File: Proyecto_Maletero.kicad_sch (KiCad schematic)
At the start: 28 parts, among them J2 Conn_01x02, J3 Conn_01x02, J4 Conn_01x03, J5 Conn_01x02, J6 Conn_01x02, J7 Conn_01x03, SW1 SW_Push, SW2 SW_SPDT, U1 LT1117-ADJ, U2 MCP2551-I-SN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

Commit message: Correccion de errores
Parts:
- removed SW2: SW_SPDT, symbol Switch:SW_SPDT
- added J8: Conn_01x02, symbol Connector_Generic:Conn_01x02
- added SW3: SW_SPST, symbol Switch:SW_SPST
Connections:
- net VRth: now also J8.1 (Pin_1), SW3.2 (B)
- net Vin: now reaches R1.2
- net Vin: now also J8.2 (Pin_2), SW3.1 (A)
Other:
- note added: "Pines switch calefactor"
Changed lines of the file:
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@@
 		)
 	)
+	(text "Pines switch \ncalefactor"
+		(exclude_from_sim no)
+		(at 116.332 30.988 0)
+		(effects
+			(font
+				(size 1.27 1.27)
+			)
+		)
+	)
 	(text "Activar Rth"
 		(exclude_from_sim no)
@@
 	)
 	(junction
+		(at 166.37 184.15)
+		(diameter 0)
+		(color 0 0 0 0)
+	)
+	(junction
 		(at 102.87 83.82)
 		(diameter 0)
@@
 	)
 	(junction
+		(at 156.21 184.15)
+		(diameter 0)
+		(color 0 0 0 0)
+	)
+	(junction
 		(at 107.95 83.82)
 		(diameter 0)
@@
 	(wire
 		(pts
+			(xy 166.37 184.15) (xy 166.37 179.07)
+		)
+		(stroke
+			(width 0)
+			(type default)
+		)
+	)
+	(wire
+		(pts
 			(xy 199.39 30.48) (xy 207.01 30.48)
 		)
@@
 	(wire
 		(pts
+			(xy 166.37 184.15) (xy 168.91 184.15)
+		)
+		(stroke
+			(width 0)
+			(type default)
+		)
+	)
+	(wire
+		(pts
 			(xy 119.38 102.87) (xy 120.65 102.87)
 		)
@@
 	(wire
 		(pts
-			(xy 166.37 181.61) (xy 168.91 181.61)
+			(xy 24.13 29.21) (xy 29.21 29.21)
 		)
 		(stroke
@@
 	(wire
 		(pts
-			(xy 24.13 29.21) (xy 29.21 29.21)
+			(xy 156.21 187.96) (xy 156.21 184.15)
 		)
 		(stroke
@@
 		)
 	)
+	(global_label "Vin"
+		(shape output)
+		(at 156.21 187.96 270)
+		(fields_autoplaced yes)
+		(effects
+			(font
+				(size 1.27 1.27)
+			)
+			(justify right)
+		)
+		(property "Intersheetrefs" "${INTERSHEET_REFS}"
+			(at 156.21 193.7876 90)
+			(effects
+				(font
+					(size 1.27 1.27)
+				)
+				(justify right)
+				(hide yes)
+			)
+		)
+	)
 	(global_label "Osc_1"
 		(shape bidirectional)
@@
 		)
 	)
+	(global_label "Vsw"
+		(shape input)
+		(at 102.87 31.75 0)
+		(fields_autoplaced yes)
+		(effects
+			(font
+				(size 1.27 1.27)
+			)
+			(justify left)
+		)
+		(property "Intersheetrefs" "${INTERSHEET_REFS}"
+			(at 109.3024 31.75 0)
+			(effects
+				(font
+					(size 1.27 1.27)
+				)
+				(justify left)
+				(hide yes)
+			)
+		)
+	)
+	(global_label "Vin"
+		(shape input)
+		(at 102.87 29.21 0)
+		(fields_autoplaced yes)
+		(effects
+			(font
+				(size 1.27 1.27)
+			)
+			(justify left)
+		)
+		(property "Intersheetrefs" "${INTERSHEET_REFS}"
+			(at 108.6976 29.21 0)
+			(effects
+				(font
+					(size 1.27 1.27)
+				)
+				(justify left)
+				(hide yes)
+			)
+		)
+	)
 	(global_label "VCC"
 		(shape output)
@@
 	(global_label "VRth"
 		(shape output)
-		(at 168.91 181.61 0)
+		(at 168.91 184.15 0)
 		(fields_autoplaced yes)
 		(effects
@@
 		)
 		(property "Intersheetrefs" "${INTERSHEET_REFS}"
-			(at 176.1285 181.61 0)
+			(at 176.1285 184.15 0)
 			(effects
 				(font
@@
 		)
 	)
+	(global_label "Vsw"
+		(shape output)
+		(at 166.37 179.07 90)
+		(fields_autoplaced yes)
+		(effects
+			(font
+				(size 1.27 1.27)
+			)
+			(justify left)
+		)
+		(property "Intersheetrefs" "${INTERSHEET_REFS}"
+			(at 166.37 172.6376 90)
+			(effects
+				(font
+					(size 1.27 1.27)
+				)
+				(justify left)
+				(hide yes)
+			)
+		)
+	)
 	(global_label "Clock_I2C"
 		(shape bidirectional)
@@
 	)
 	(symbol
+		(lib_id "Connector_Generic:Conn_01x02")
+		(at 97.79 31.75 180)
+		(unit 1)
+		(exclude_from_sim no)
+		(in_bom yes)
+		(on_board yes)
+		(dnp no)
+		(fields_autoplaced yes)
+		(property "Reference" "J8"
+			(at 97.79 22.86 0)
+			(effects
+				(font
+					(size 1.27 1.27)
+				)
+			)
+		)
+		(property "Value" "Conn_01x02"
+			(at 97.79 25.4 0)
+			(effects
+				(font
+					(size 1.27 1.27)
+				)
+			)
+		)
+		(property "Footprint" ""
+			(at 97.79 31.75 0)
+			(effects
+				(font
+					(size 1.27 1.27)
+				)
+				(hide yes)
+			)
+		)
+		(property "Datasheet" "~"
+			(at 97.79 31.75 0)
+			(effects
+				(font
+					(size 1.27 1.27)
+				)
+				(hide yes)
+			)
+		)
+		(property "Description" "Generic connector, single row, 01x02, script generated (kicad-library-utils/schlib/autogen/connector/)"
+			(at 97.79 31.75 0)
+			(effects
+				(font
+					(size 1.27 1.27)
+				)
+				(hide yes)
+			)
+		)
+		(pin "1"
+		)
+		(pin "2"
+		)
+		(instances
+			(project "Proyecto_Maletero"
+				(path "/14c0d961-a62d-4b1a-b8ec-37f60ffee5fd"
+					(reference "J8")
+					(unit 1)
+				)
+			)
+		)
+	)
+	(symbol
 		(lib_id "Regulator_Linear:LT1117-ADJ")
 		(at 226.06 30.48 0)
@@
 		(on_board yes)
 		(dnp no)
-		(fields_autoplaced yes)
 		(property "Reference" "C6"
 			(at 115.57 144.7799 0)
@@
 		)
 		(property "Value" "15pF"
-			(at 115.57 147.3199 0)
+			(at 114.3 147.32 0)
 			(effects
 				(font
@@
 		(on_board yes)
 		(dnp no)
-		(fields_autoplaced yes)
 		(property "Reference" "C7"
-			(at 102.87 144.7799 0)
+			(at 94.742 144.78 0)
 			(effects
 				(font
@@
 		)
 		(property "Value" "15pF"
-			(at 102.87 147.3199 0)
+			(at 93.98 148.336 0)
 			(effects
 				(font
@@
 	)
 	(symbol
-		(lib_id "Switch:SW_SPDT")
-		(at 161.29 184.15 0)
-		(unit 1)
-		(exclude_from_sim no)
-		(in_bom yes)
-		(on_board yes)
-		(dnp no)
-		(fields_autoplaced yes)
-		(property "Reference" "SW2"
-			(at 161.29 175.26 0)
-			(effects
-				(font
-					(size 1.27 1.27)
-				)
-			)
-		)
-		(property "Value" "SW_SPDT"
-			(at 161.29 177.8 0)
-			(effects
-				(font
-					(size 1.27 1.27)
-				)
-			)
-		)
-		(property "Footprint" ""
-			(at 161.29 184.15 0)
-			(effects
-				(font
-					(size 1.27 1.27)
-				)
-				(hide yes)
-			)
-		)
-		(property "Datasheet" "~"
-			(at 161.29 191.77 0)
-			(effects
-				(font
-					(size 1.27 1.27)
-				)
-				(hide yes)
-			)
-		)
-		(property "Description" "Switch, single pole double throw"
-			(at 161.29 184.15 0)
-			(effects
-				(font
-					(size 1.27 1.27)
-				)
-				(hide yes)
-			)
-		)
-		(pin "1"
-		)
-		(pin "2"
-		)
-		(pin "3"
-		)
-		(instances
-			(project ""
-				(path "/14c0d961-a62d-4b1a-b8ec-37f60ffee5fd"
-					(reference "SW2")
-					(unit 1)
-				)
-			)
-		)
-	)
-	(symbol
 		(lib_id "power:GND")
 		(at 29.21 58.42 0)
@@
 	)
 	(symbol
-		(lib_id "power:GND")
-		(at 166.37 186.69 0)
+		(lib_id "Switch:SW_SPST")
+		(at 161.29 184.15 0)
 		(unit 1)
 		(exclude_from_sim no)
@@
 		(on_board yes)
 		(dnp no)
-		(property "Reference" "#PWR015"
-			(at 166.37 193.04 0)
+		(fields_autoplaced yes)
+		(property "Reference" "SW3"
+			(at 161.29 177.8 0)
 			(effects
 				(font
 					(size 1.27 1.27)
 				)
-				(hide yes)
 			)
 		)
-		(property "Value" "GND"
-			(at 166.37 190.5 0)
+		(property "Value" "SW_SPST"
+			(at 161.29 180.34 0)
 			(effects
 				(font
@@
 		)
 		(property "Footprint" ""
-			(at 166.37 186.69 0)
+			(at 161.29 184.15 0)
 			(effects
 				(font
@@
 			)
 		)
-		(property "Datasheet" ""
-			(at 166.37 186.69 0)
+		(property "Datasheet" "~"
+			(at 161.29 184.15 0)
 			(effects
 				(font
@@
 			)
 		)
-		(property "Description" "Power symbol creates a global label with name \"GND\" , ground"
-			(at 166.37 186.69 0)
+		(property "Description" "Single Pole Single Throw (SPST) switch"
+			(at 161.29 184.15 0)
 			(effects
 				(font
@@
 		(pin "1"
 		)
+		(pin "2"
+		)
 		(instances
 			(project ""
 				(path "/14c0d961-a62d-4b1a-b8ec-37f60ffee5fd"
-					(reference "#PWR015")
+					(reference "SW3")
 					(unit 1)
 				)

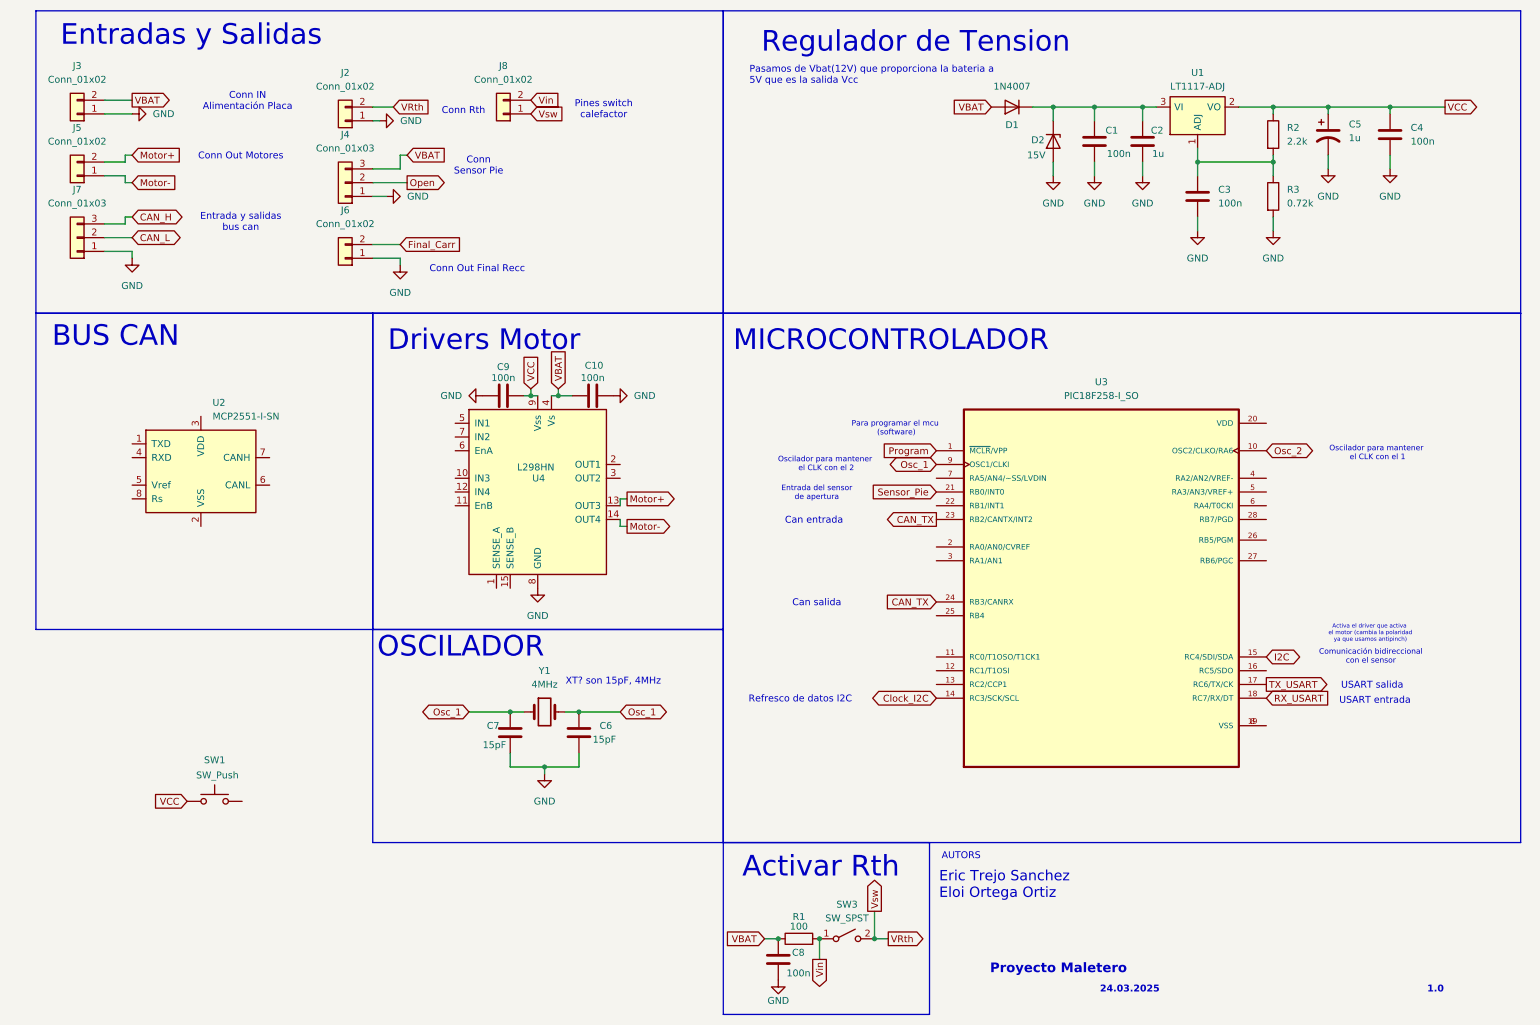
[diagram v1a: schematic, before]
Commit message: Transcriver CAN, caso todo mcu
Falta final de carrera
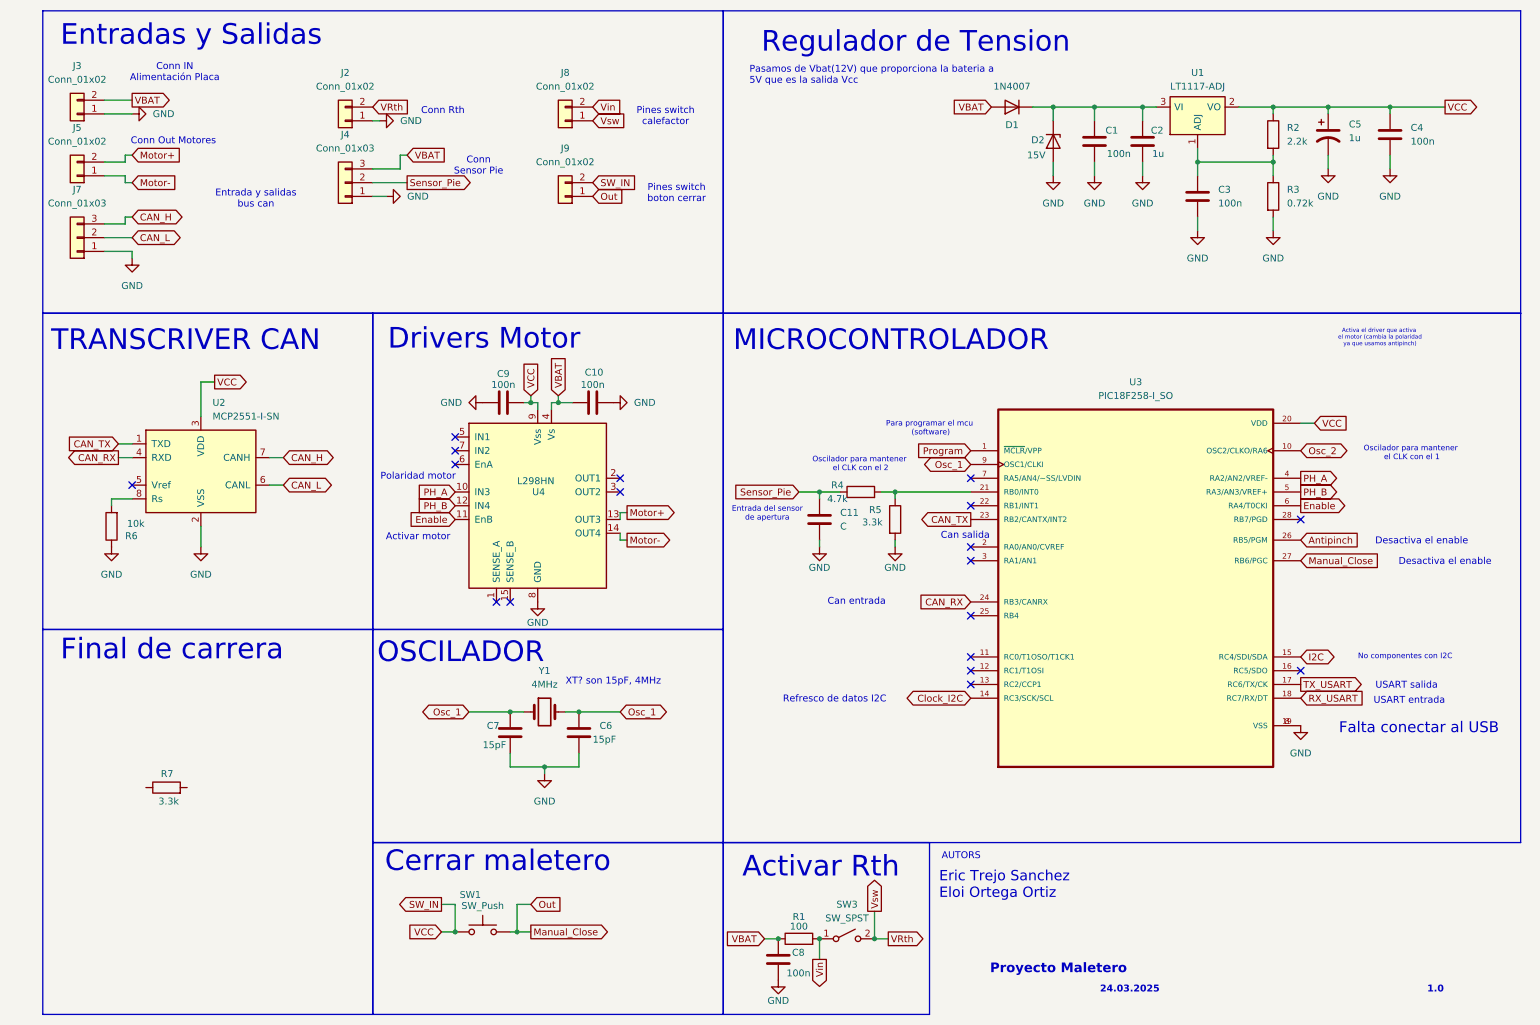
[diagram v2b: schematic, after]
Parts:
- removed J6: Conn_01x02, TerminalBlock_Phoenix:TerminalBlock_Phoenix_MKDS-1,5-2-5.08_1x02_P5.08mm_Horizontal, symbol Connector_Generic:Conn_01x02
- added C11: C, symbol Device:C
- added J9: Conn_01x02, symbol Connector_Generic:Conn_01x02
- added R4: 4.7k, symbol Device:R
- added R5, R7: 3.3k, symbol Device:R
- added R6: 10k, symbol Device:R
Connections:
- net Open is gone; now on net Sensor_Pie: J4.2 (Pin_2)
- net VCC is gone; now on net SW_IN: C4.1, C5.1, C9.2, R2.1, SW1.1, U1.2 (VO), U4.9 (Vss)
- net CAN_H: now also U2.7 (CANH)
- net CAN_L: now also U2.6 (CANL)
- net CAN_TX: now also U2.1 (TXD); no longer U3.24 (RB3/CANRX)
- net GND: now also U2.2 (VSS), U3.19 (VSS), U3.8 (VSS), C11.2, R5.2, R6.1
- net Sensor_Pie: now also C11.1, R4.1; no longer U3.21 (RB0/INT0)
- net SW_IN: now reaches U2.3 (VDD)
- net SW_IN: now also U3.20 (VDD), J9.2 (Pin_2)
- net CAN_RX: now reaches U2.4 (RXD)
- net CAN_RX: now also U3.24 (RB3/CANRX)
- net at U2.8 (Rs): now also R6.2
- net Manual_Close: now reaches SW1.2
- net Manual_Close: now also U3.27 (RB6/PGC), J9.1 (Pin_1)
- net PH_A: now reaches U4.10 (IN3)
- net PH_A: now also U3.4 (RA2/AN2/VREF-)
- net Enable: now reaches U4.11 (EnB)
- net Enable: now also U3.6 (RA4/T0CKI)
- net PH_B: now reaches U4.12 (IN4)
- net PH_B: now also U3.5 (RA3/AN3/VREF+)
- net Antipinch: now reaches U3.26 (RB5/PGM)
- new net: R4.2, R5.1, U3.21 (RB0/INT0)
- no-connect marks 0 -> 18
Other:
- note added: "Activar motor"
- note added: "Cerrar maletero"
- note added: "Desactiva el enable"
- note added: "Falta conectar al USB"
- note added: "Final de carrera"
- note added: "No componentes con I2C"
- note added: "Pines switch boton cerrar"
- note added: "Polaridad motor"
- note added: "TRANSCRIVER CAN"
- note removed: "BUS CAN"
- note removed: "Comunicación bidireccional con el sensor"
- note removed: "Conn Out Final Recc"
- moved on the sheet: C10, C9, J8, SW1, U3, U4
